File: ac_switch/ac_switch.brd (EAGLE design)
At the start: 34.3 x 79.8 mm, 23 parts, among them IC1 TINY85, T1 BC337

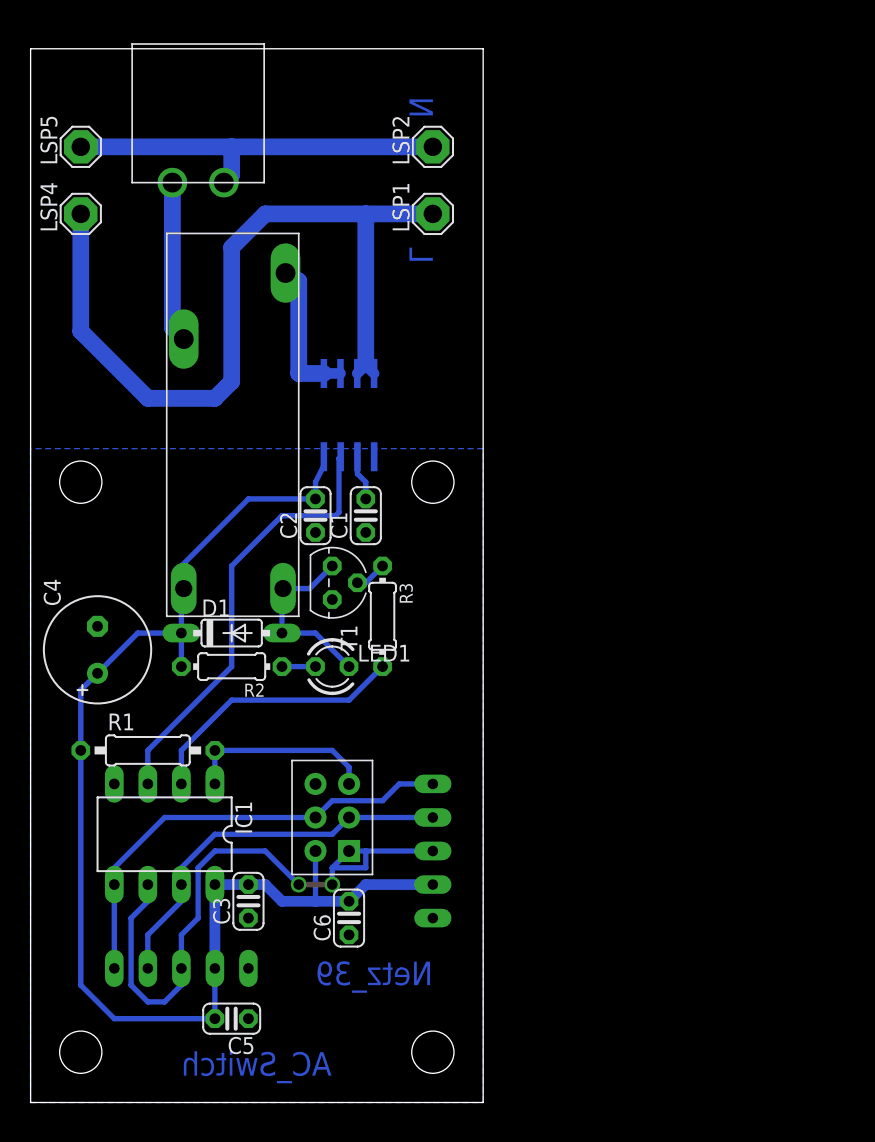
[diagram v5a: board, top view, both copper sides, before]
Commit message: Positionen der Lötpunkte für AC angepasst, sodass die Boards zueinander passen mehr Platz um die Lötbrücke
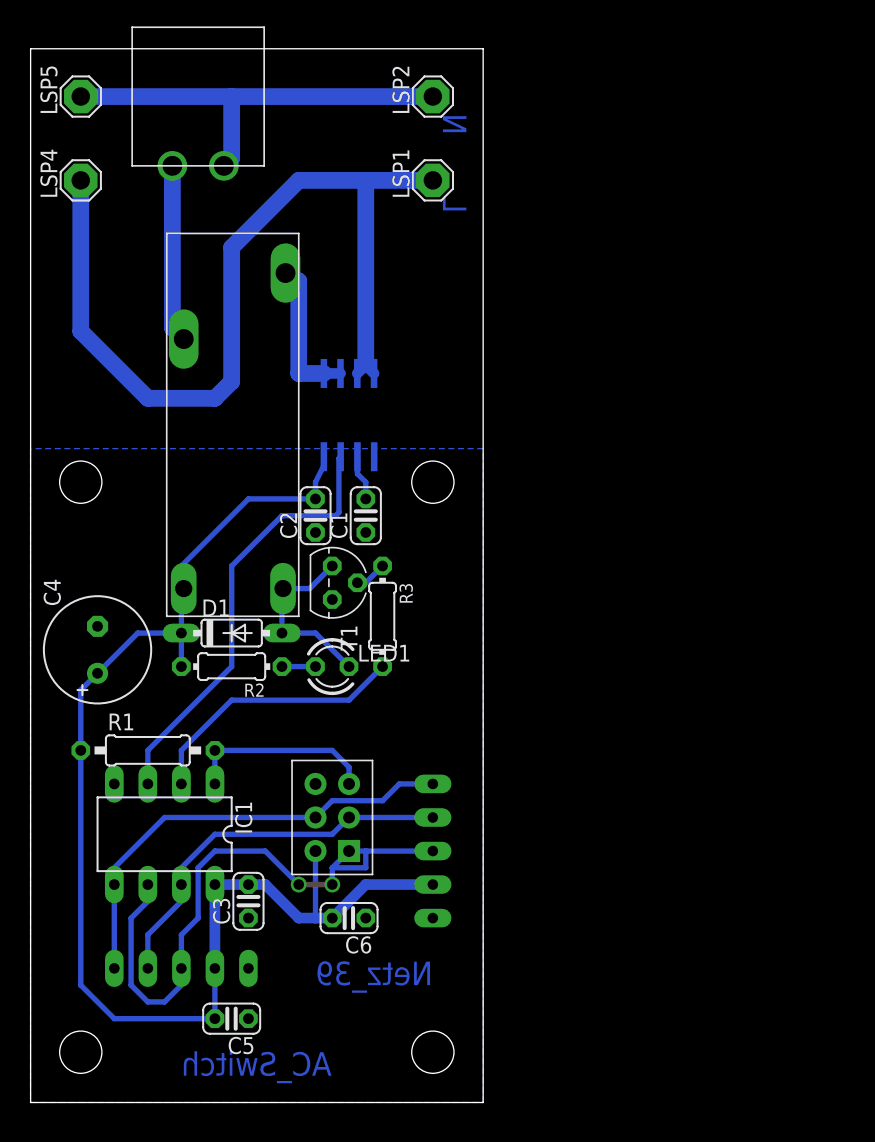
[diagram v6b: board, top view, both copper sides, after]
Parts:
- moved LSP2 3.81 mm to (30.5, 76.2)
- moved LSP5 3.81 mm to (3.81, 76.2)
- moved LSP1 2.54 mm to (30.5, 69.8)
- moved LSP4 2.54 mm to (3.81, 69.8)
- moved U$6 1.27 mm to (12.7, 76.2)
- turned C6 to 180 degrees
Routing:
- net L: track 62.7 -> 68.8 mm
- net N: track 29.6 -> 32.2 mm
- net VCC: track 97.9 -> 100.2 mm
- net L_OUT: track 12.2 -> 13.5 mm
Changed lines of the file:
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@@
 <wire x1="0.01" y1="79.82" x2="0.01" y2="0" width="0" layer="20"/>
 <wire x1="0.01" y1="0" x2="34.29" y2="0" width="0" layer="20"/>
-<text x="30.48" y="76.2" size="1.778" layer="16" font="vector" rot="MR270">N</text>
-<text x="30.48" y="64.77" size="1.778" layer="16" font="vector" rot="MR270">L</text>
+<text x="33.02" y="74.93" size="1.778" layer="16" font="vector" rot="MR270">N</text>
+<text x="33.02" y="68.58" size="1.778" layer="16" font="vector" rot="MR270">L</text>
 <text x="30.48" y="8.89" size="1.778" layer="16" font="vector" rot="MR0">Netz_39</text>
 <text x="11.43" y="3.81" size="1.778" layer="16" font="vector" rot="MR180">AC_Switch</text>
@@
 <element name="U$3" library="n39" package="I3C_PADS" value="I3C_PORT" x="11.43" y="10.16" rot="R270"/>
 <element name="U$4" library="n39" package="AVR_ISP" value="AVR_ISP" x="22.86" y="21.59" rot="R180"/>
-<element name="LSP1" library="solpad" package="SE14" value="SE14" x="30.48" y="67.31" rot="R90"/>
-<element name="LSP2" library="solpad" package="SE14" value="SE14" x="30.48" y="72.39" rot="R90"/>
-<element name="LSP4" library="solpad" package="SE14" value="SE14" x="3.81" y="67.31" rot="R90"/>
-<element name="LSP5" library="solpad" package="SE14" value="SE14" x="3.81" y="72.39" rot="R90"/>
+<element name="LSP1" library="solpad" package="SE14" value="SE14" x="30.48" y="69.85" rot="R90"/>
+<element name="LSP2" library="solpad" package="SE14" value="SE14" x="30.48" y="76.2" rot="R90"/>
+<element name="LSP4" library="solpad" package="SE14" value="SE14" x="3.81" y="69.85" rot="R90"/>
+<element name="LSP5" library="solpad" package="SE14" value="SE14" x="3.81" y="76.2" rot="R90"/>
 <element name="C4" library="resistor" package="E3,5-8" value="68µ" x="5.08" y="34.29" rot="R90"/>
 <element name="U$5" library="n39" package="I3C_PADS" value="I3C_PORT" x="30.48" y="19.05" rot="R180"/>
 <element name="R3" library="resistor" package="0204/7" value="1,5K" x="26.67" y="36.83" rot="R270"/>
-<element name="U$6" library="n39" package="WAGO_734_262" value="WAGO_734_262" x="12.7" y="74.93"/>
+<element name="U$6" library="n39" package="WAGO_734_262" value="WAGO_734_262" x="12.7" y="76.2"/>
 <element name="C5" library="resistor" package="C025-024X044" value="100n" x="15.24" y="6.35" rot="R180"/>
-<element name="C6" library="resistor" package="C025-024X044" value="100n" x="24.13" y="13.97" rot="R90"/>
+<element name="C6" library="resistor" package="C025-024X044" value="100n" x="24.13" y="13.97" rot="R180"/>
 </elements>
 <signals>
@@
 <wire x1="13.97" y1="16.51" x2="16.51" y2="16.51" width="0.8128" layer="16"/>
 <wire x1="22.225" y1="48.26" x2="22.225" y2="48.916" width="0.4064" layer="16"/>
-<wire x1="24.13" y1="15.24" x2="21.59" y2="15.24" width="0.8128" layer="16"/>
-<wire x1="21.59" y1="15.24" x2="19.05" y2="15.24" width="0.8128" layer="16"/>
-<wire x1="19.05" y1="15.24" x2="17.78" y2="16.51" width="0.8128" layer="16"/>
+<wire x1="21.59" y1="13.97" x2="20.32" y2="13.97" width="0.8128" layer="16"/>
+<wire x1="20.32" y1="13.97" x2="17.78" y2="16.51" width="0.8128" layer="16"/>
 <wire x1="17.78" y1="16.51" x2="16.51" y2="16.51" width="0.8128" layer="16"/>
 <wire x1="13.97" y1="16.51" x2="13.97" y2="10.16" width="0.8128" layer="16"/>
@@
 <wire x1="6.35" y1="6.35" x2="3.81" y2="8.89" width="0.4064" layer="16"/>
 <wire x1="3.81" y1="8.89" x2="3.81" y2="26.67" width="0.4064" layer="16"/>
-<wire x1="21.59" y1="19.05" x2="21.59" y2="15.24" width="0.4064" layer="16"/>
+<wire x1="21.59" y1="19.05" x2="21.59" y2="13.97" width="0.4064" layer="16"/>
 <contactref element="U$1" pad="P$2"/>
 <contactref element="R2" pad="2"/>
@@
 <contactref element="C5" pad="2"/>
 <contactref element="C6" pad="2"/>
-<wire x1="24.13" y1="15.24" x2="25.4" y2="16.51" width="0.8128" layer="16"/>
+<wire x1="22.86" y1="13.97" x2="25.4" y2="16.51" width="0.8128" layer="16"/>
 <wire x1="25.4" y1="16.51" x2="30.48" y2="16.51" width="0.8128" layer="16"/>
+<wire x1="21.59" y1="13.97" x2="22.86" y2="13.97" width="0.8128" layer="16"/>
 </signal>
 <signal name="N$1">
@@
 <contactref element="LSP2" pad="MP"/>
 <contactref element="LSP5" pad="MP"/>
-<wire x1="3.81" y1="72.39" x2="15.24" y2="72.39" width="1.27" layer="16"/>
+<wire x1="3.81" y1="76.2" x2="15.24" y2="76.2" width="1.27" layer="16"/>
 <contactref element="U$6" pad="P$2"/>
-<wire x1="15.24" y1="72.39" x2="30.48" y2="72.39" width="1.27" layer="16"/>
-<wire x1="14.65" y1="69.68" x2="15.24" y2="70.27" width="1.27" layer="16"/>
-<wire x1="15.24" y1="70.27" x2="15.24" y2="72.39" width="1.27" layer="16"/>
+<wire x1="15.24" y1="76.2" x2="30.48" y2="76.2" width="1.27" layer="16"/>
+<wire x1="14.65" y1="70.95" x2="15.24" y2="71.54" width="1.27" layer="16"/>
+<wire x1="15.24" y1="71.54" x2="15.24" y2="76.2" width="1.27" layer="16"/>
 </signal>
 <signal name="N$3">
@@
 <contactref element="LSP1" pad="MP"/>
 <contactref element="LSP4" pad="MP"/>
-<wire x1="30.48" y1="67.31" x2="25.4" y2="67.31" width="1.27" layer="16"/>
-<wire x1="25.4" y1="67.31" x2="17.78" y2="67.31" width="1.27" layer="16"/>
-<wire x1="17.78" y1="67.31" x2="15.24" y2="64.77" width="1.27" layer="16"/>
+<wire x1="30.48" y1="69.85" x2="25.4" y2="69.85" width="1.27" layer="16"/>
+<wire x1="25.4" y1="69.85" x2="20.32" y2="69.85" width="1.27" layer="16"/>
+<wire x1="20.32" y1="69.85" x2="15.24" y2="64.77" width="1.27" layer="16"/>
 <wire x1="15.24" y1="64.77" x2="15.24" y2="54.61" width="1.27" layer="16"/>
 <wire x1="15.24" y1="54.61" x2="13.97" y2="53.34" width="1.27" layer="16"/>
 <wire x1="13.97" y1="53.34" x2="8.89" y2="53.34" width="1.27" layer="16"/>
 <wire x1="8.89" y1="53.34" x2="3.81" y2="58.42" width="1.27" layer="16"/>
-<wire x1="3.81" y1="58.42" x2="3.81" y2="67.31" width="1.27" layer="16"/>
+<wire x1="3.81" y1="58.42" x2="3.81" y2="69.85" width="1.27" layer="16"/>
 <contactref element="U$2" pad="3"/>
 <contactref element="U$2" pad="4"/>
 <wire x1="26.025" y1="55.224" x2="25.4" y2="55.849" width="0.8128" layer="16"/>
 <wire x1="25.4" y1="55.849" x2="25.4" y2="55.869" width="0.8128" layer="16"/>
-<wire x1="25.4" y1="55.88" x2="25.4" y2="67.31" width="1.27" layer="16"/>
+<wire x1="25.4" y1="55.88" x2="25.4" y2="69.85" width="1.27" layer="16"/>
 <wire x1="24.755" y1="55.224" x2="25.4" y2="55.869" width="0.8128" layer="16"/>
 <wire x1="25.4" y1="55.869" x2="25.4" y2="55.88" width="0.8128" layer="16"/>
@@
 <contactref element="U$6" pad="P$1"/>
 <wire x1="11.61" y1="57.83" x2="10.75" y2="58.69" width="1.27" layer="16"/>
-<wire x1="10.75" y1="58.69" x2="10.75" y2="69.68" width="1.27" layer="16"/>
+<wire x1="10.75" y1="58.69" x2="10.75" y2="70.95" width="1.27" layer="16"/>
 </signal>
 <signal name="N$4">

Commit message: AC switch: re-routing
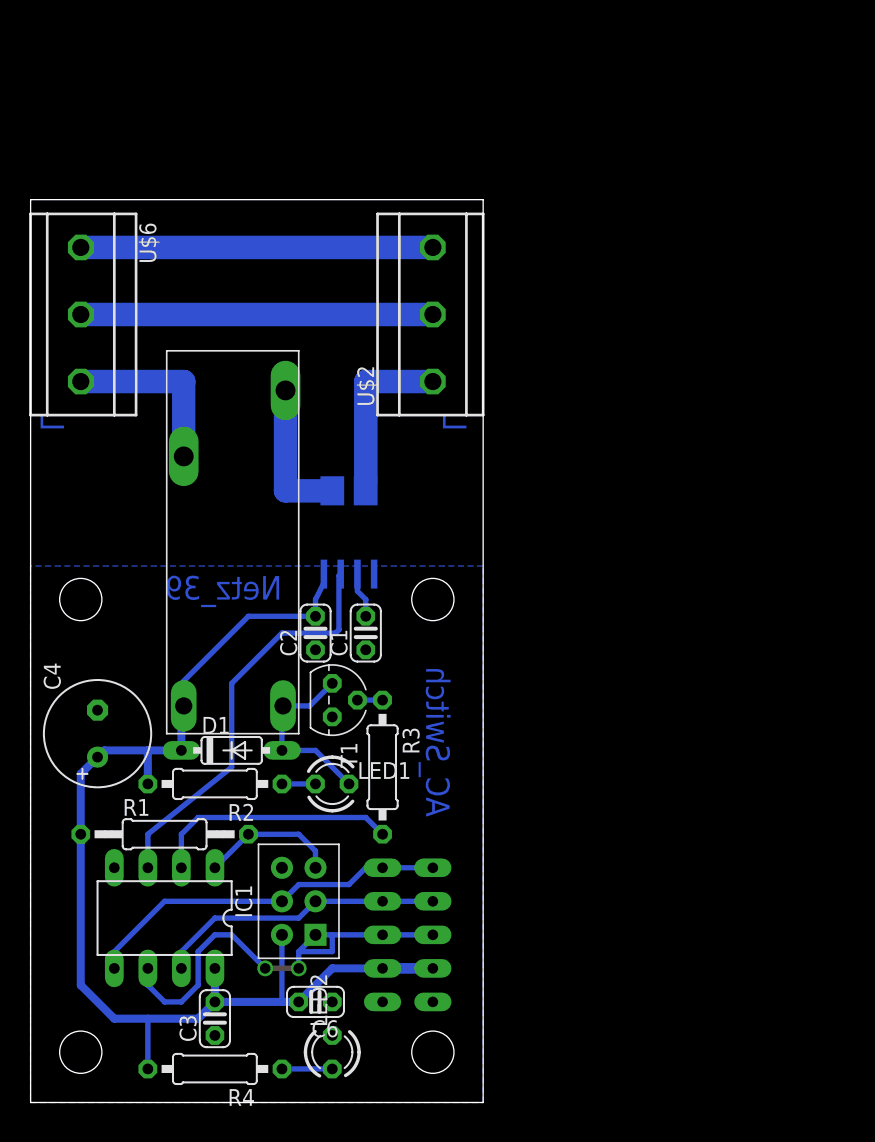
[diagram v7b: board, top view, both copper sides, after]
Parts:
- removed C5: 100n, resistor:C025-024X044
- removed LSP1, LSP2, LSP4, LSP5: SE14, solpad:SE14
- added IC2: ACS714, n39:ACS714
- added LED2: gn, led:LED3MM
- added R4: 220R, resistor:0207/10
- LED1: value (none) -> bl
- R1: device resistor:0207/10 -> resistor:0207/12
- R2: value 220R -> 470R; device resistor:0204/7 -> resistor:0207/10
- R3: device resistor:0204/7 -> resistor:0207/10
- U$2: value ASC714 -> RIACON_101_3; device n39:SOIC8 -> n39:RIACON_101_3
- U$6: value WAGO_734_262 -> RIACON_101_3; device n39:WAGO_734_262 -> n39:RIACON_101_3
- moved U$3 19.2 mm to (30.5, 12.7), turned to 180 degrees
- moved U$6 18.8 mm to (3.81, 59.7), turned to 270 degrees
- moved R3 11.4 mm to (26.7, 25.4)
- moved U$2 9.92 mm to (30.5, 59.7), flipped to the top, turned to 90 degrees
- moved C3 9.25 mm to (14.0, 6.35)
- moved R2 8.98 mm to (14.0, 24.1)
- moved LED1 8.89 mm to (22.9, 24.1)
- moved C1 8.89 mm to (25.4, 35.6)
- moved C2 8.89 mm to (21.6, 35.6)
- moved D1 8.89 mm to (15.2, 26.7)
- moved T1 8.89 mm to (22.9, 30.5)
- moved U$1 8.89 mm to (20.3, 27.9)
- moved U$5 7.41 mm to (26.7, 12.7)
- moved C6 6.84 mm to (21.6, 7.62)
- moved U$4 6.84 mm to (20.3, 15.2)
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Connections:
- removed net N: LSP2.MP, LSP5.MP, U$6.P$2
- new net N$6: LED2.A, R4.1
- new net N$8: U$2.3, U$6.1
- new net N$9: U$2.2, U$6.2
- net GND: now also IC2.5, LED2.K; no longer C5.1, U$2.5
- net L: now also IC2.3-4, U$2.1; no longer LSP1.MP, LSP4.MP, U$2.3, U$2.4
- net L_OUT: now also U$6.3; no longer U$6.P$1
- net N$2: now also IC2.6; no longer U$2.6
- net N$3: now also IC2.1-2; no longer U$2.1, U$2.2
- net SENSE: now also IC2.7; no longer U$2.7
- net VCC: now also IC2.8, R4.2; no longer C5.2, U$2.8
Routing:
- net L: track 68.8 -> 13.4 mm
- net N: track 32.2 -> 0.00 mm
- net N$9: track 0.00 -> 26.7 mm
- net N$8: track 0.00 -> 26.7 mm
- net REQ: track 47.4 -> 33.6 mm
- net VCC: track 100.2 -> 88.5 mm
- net SCL: track 29.3 -> 21.9 mm
- net SDA: track 34.4 -> 28.0 mm
- net RST: track 14.5 -> 10.5 mm
- net N$6: track 0.00 -> 3.81 mm
- net SENSE: track 33.2 -> 31.1 mm
- net SWITCH: track 20.4 -> 18.8 mm
- net N$5: track 2.43 -> 1.91 mm
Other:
- board size 34.3 x 79.8 mm -> 34.3 x 68.4 mm
- board text removed: "N"

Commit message: Added a fuse and an OP amp to increase signal bandwith.
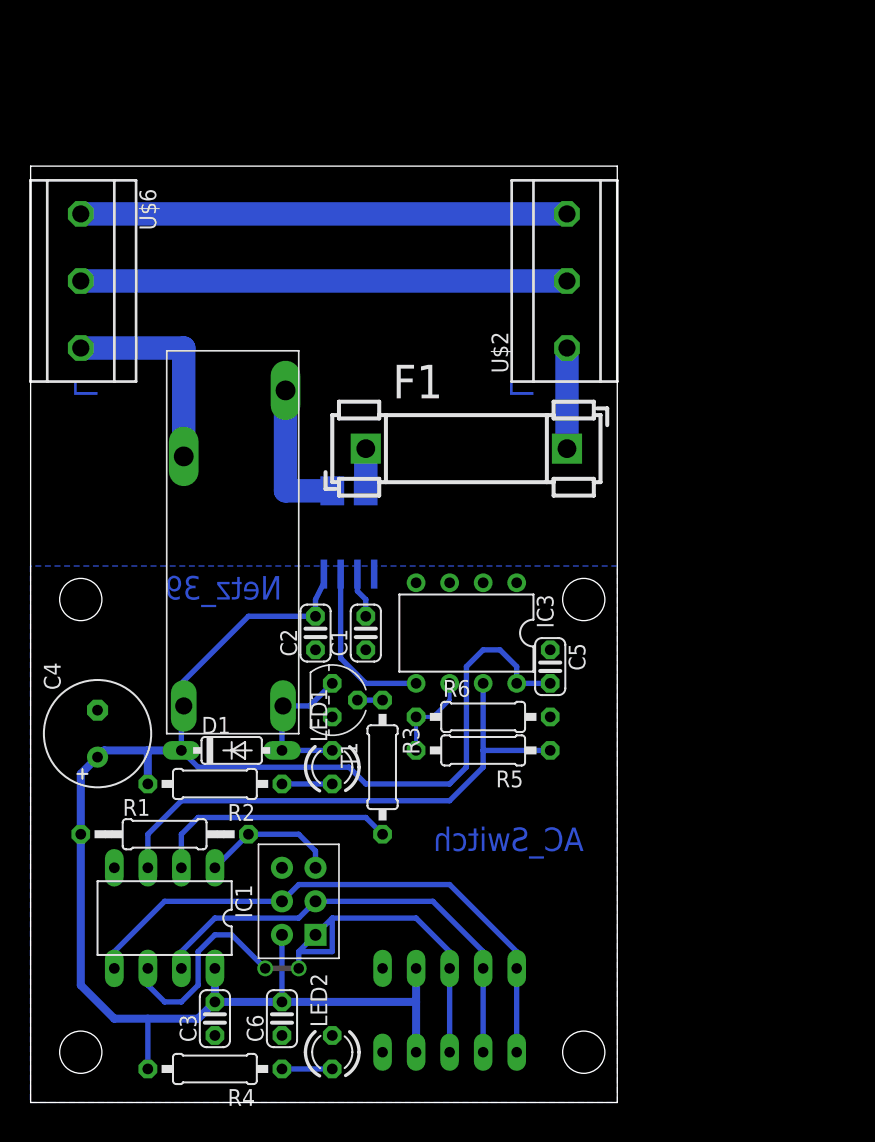
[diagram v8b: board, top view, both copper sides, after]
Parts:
- added C5: 100n, resistor:C025-024X044
- added F1: FUSEBLANK_5X20MM, fuse:FUSE_HOLDER_5X20MM
- added IC3: LM1458N, linear:DIL08
- added R5: 10K, resistor:0207/10
- added R6: 1,5K, resistor:0207/10
- moved U$2 10.5 mm to (40.6, 62.2)
- moved U$3 8.98 mm to (31.8, 3.81), turned to 90 degrees
- moved U$5 5.68 mm to (31.8, 10.2), turned to 90 degrees
- moved C6 2.84 mm to (19.1, 6.35), turned to 90 degrees
- moved U$6 2.54 mm to (3.81, 62.2)
- moved LED1 1.27 mm to (22.9, 25.4), turned to 90 degrees
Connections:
- new net CURRENT: IC1.3, IC3.7, R5.1
- new net N$10: IC3.6, R5.2, R6.1
- new net N$7: F1.1, IC2.3-4
- net GND: now also C5.1, IC3.2, IC3.3, IC3.4, R6.2
- net L: now also F1.2; no longer IC2.3-4
- net SENSE: now also IC3.5; no longer IC1.3
- net VCC: now also C5.2, IC3.8
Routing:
- net VCC: track 88.5 -> 132.0 mm
- net CURRENT: track 0.00 -> 41.5 mm
- net SENSE: track 31.1 -> 12.9 mm
- net SDA: track 28.0 -> 43.6 mm
- net SCL: track 21.9 -> 34.9 mm
- net REQ: track 33.6 -> 45.4 mm
- net N$9: track 26.7 -> 36.8 mm
- net N$8: track 26.7 -> 36.8 mm
- net N$10: track 0.00 -> 6.88 mm
- net L: track 13.4 -> 7.62 mm
- net N$7: track 0.00 -> 3.21 mm
- net L_OUT: track 13.5 -> 16.0 mm
- net N$1: track 14.0 -> 11.7 mm
- net N$4: track 2.54 -> 3.81 mm
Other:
- board size 34.3 x 68.4 mm -> 44.4 x 70.9 mm
